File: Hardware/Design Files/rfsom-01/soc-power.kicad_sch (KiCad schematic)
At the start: 55 parts

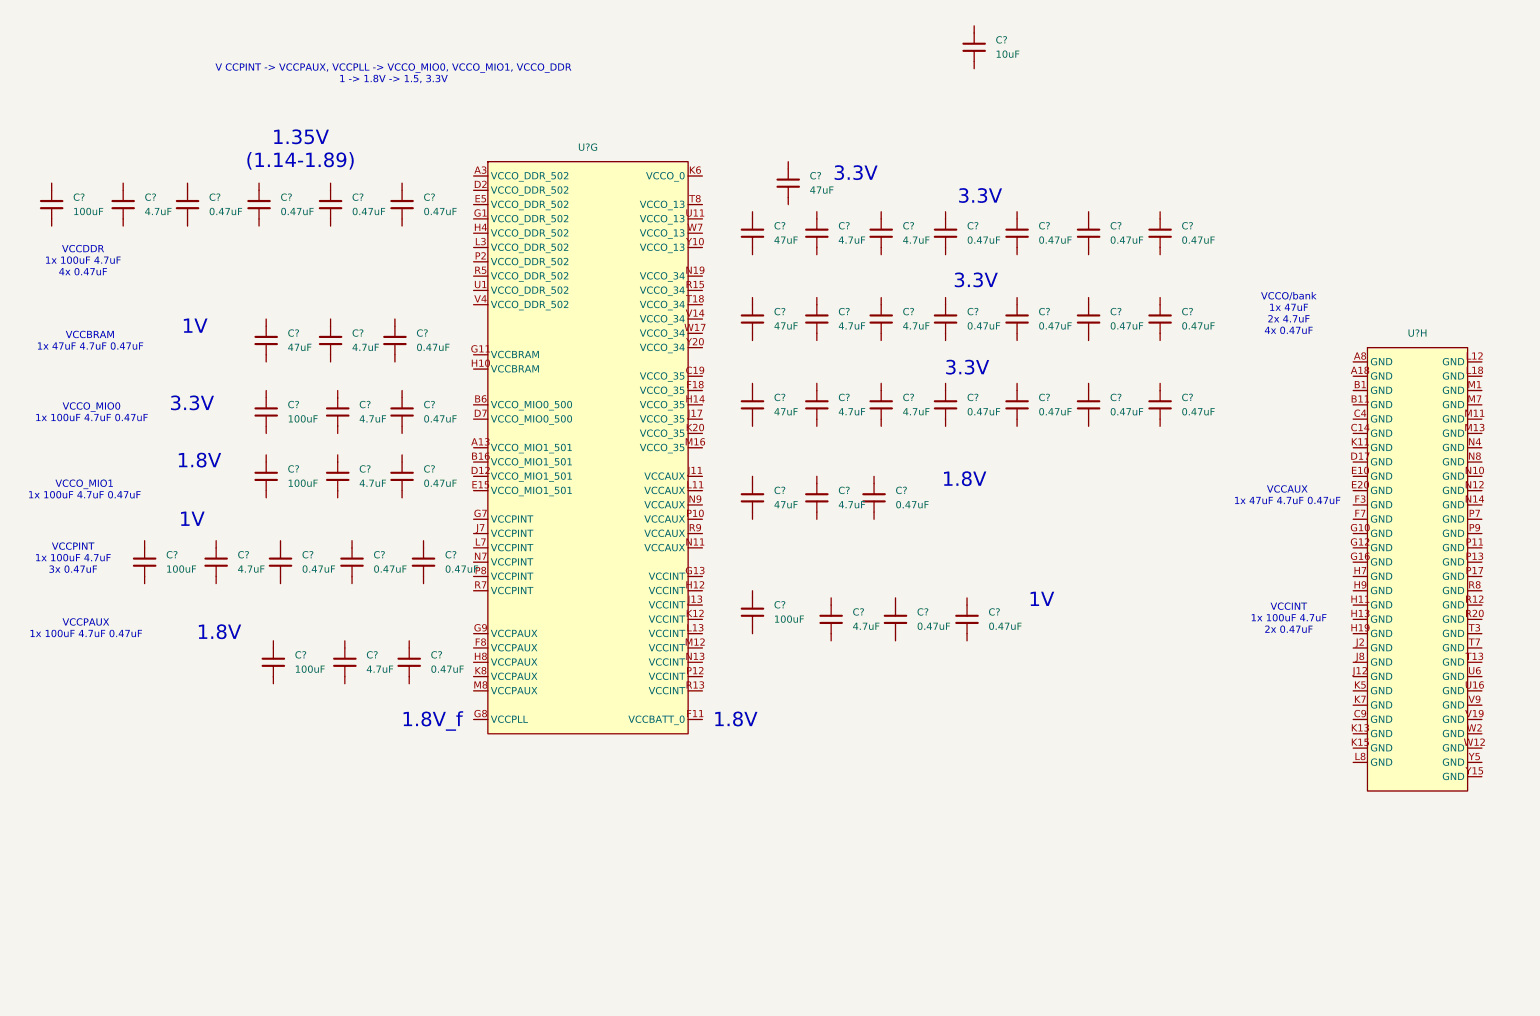
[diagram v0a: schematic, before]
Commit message: ddr progress; added more conns;
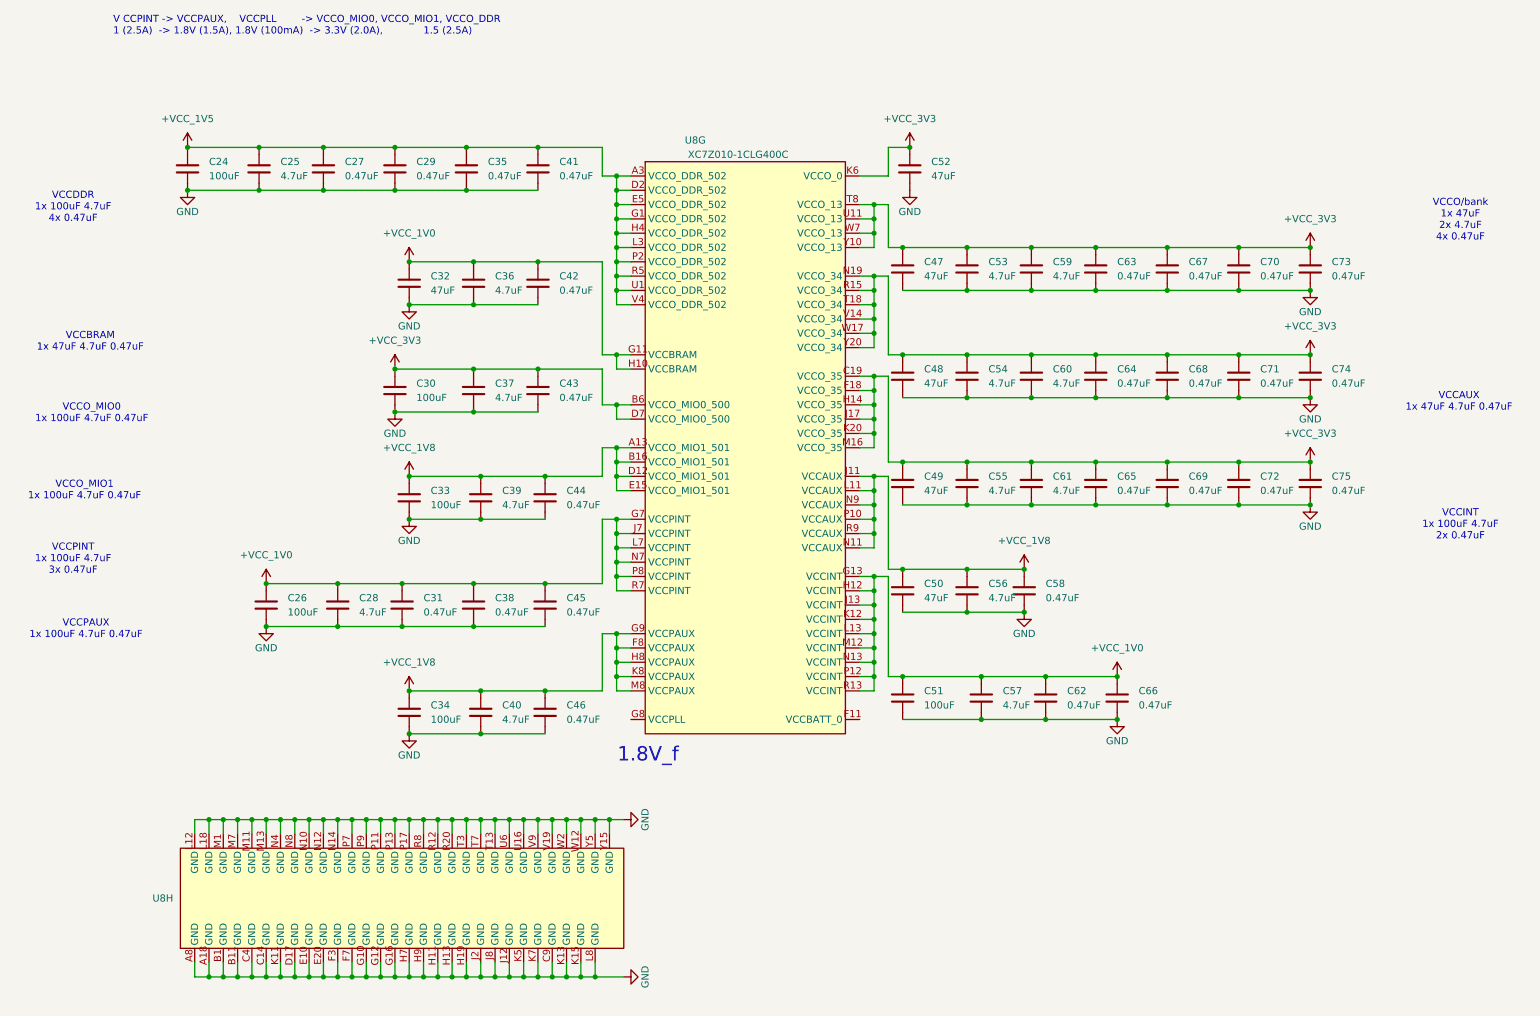
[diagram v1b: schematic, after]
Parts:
- removed C?: GRM188R60G106ME47, Capacitor_SMD:C_0603_1608Metric, symbol Capacitors:GRM188R60G106ME47
- U8: renamed from U?; footprint Package_BGA:Xilinx_CLG400 -> ICs:CLG400
- gave numbers to parts that had none: 53
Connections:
- net +VCC_3V3: now reaches C74.1
- net +VCC_3V3: now also C30.1, C37.1, C43.1, C47.1, C48.1, C49.1, C52.1, C53.1, C54.1, C55.1, C59.1, C60.1, C61.1, C63.1, C64.1, C65.1, C67.1, C68.1, C69.1, C70.1, C71.1, C72.1, C73.1, C75.1, U8.B6 (VCCO_MIO0_500), U8.C19 (VCCO_35), U8.D7 (VCCO_MIO0_500), U8.F18 (VCCO_35), U8.H14 (VCCO_35), U8.J17 (VCCO_35), U8.K20 (VCCO_35), U8.K6 (VCCO_0), U8.M16 (VCCO_35), U8.N19 (VCCO_34), U8.R15 (VCCO_34), U8.T18 (VCCO_34), U8.T8 (VCCO_13), U8.U11 (VCCO_13), U8.V14 (VCCO_34), U8.W17 (VCCO_34), U8.W7 (VCCO_13), U8.Y10 (VCCO_13), U8.Y20 (VCCO_34)
- net GND: now reaches C74.2
- net GND: now also C24.2, C25.2, C26.2, C27.2, C28.2, C29.2, C30.2, C31.2, C32.2, C33.2, C34.2, C35.2, C36.2, C37.2, C38.2, C39.2, C40.2, C41.2, C42.2, C43.2, C44.2, C45.2, C46.2, C47.2, C48.2, C49.2, C50.2, C51.2, C52.2, C53.2, C54.2, C55.2, C56.2, C57.2, C58.2, C59.2, C60.2, C61.2, C62.2, C63.2, C64.2, C65.2, C66.2, C67.2, C68.2, C69.2, C70.2, C71.2, C72.2, C73.2, C75.2, U8.A18 (GND), U8.A8 (GND), U8.B1 (GND), U8.B11 (GND), U8.C14 (GND), U8.C4 (GND), U8.C9 (GND), U8.D17 (GND), U8.E10 (GND), U8.E20 (GND), U8.F3 (GND), U8.F7 (GND), U8.G10 (GND), U8.G12 (GND), U8.G16 (GND), U8.H11 (GND), U8.H13 (GND), U8.H19 (GND), U8.H7 (GND), U8.H9 (GND), U8.J12 (GND), U8.J2 (GND), U8.J8 (GND), U8.K11 (GND), U8.K13 (GND), U8.K15 (GND), U8.K5 (GND), U8.K7 (GND), U8.L12 (GND), U8.L18 (GND), U8.L8 (GND), U8.M1 (GND), U8.M11 (GND), U8.M13 (GND), U8.M7 (GND), U8.N10 (GND), U8.N12 (GND), U8.N14 (GND), U8.N4 (GND), U8.N8 (GND), U8.P11 (GND), U8.P13 (GND), U8.P17 (GND), U8.P7 (GND), U8.P9 (GND), U8.R12 (GND), U8.R20 (GND), U8.R8 (GND), U8.T13 (GND), U8.T3 (GND), U8.T7 (GND), U8.U16 (GND), U8.U6 (GND), U8.V19 (GND), U8.V9 (GND), U8.W12 (GND), U8.W2 (GND), U8.Y15 (GND), U8.Y5 (GND)
- net +VCC_1V5: now reaches C41.1
- net +VCC_1V5: now also C24.1, C25.1, C27.1, C29.1, C35.1, U8.A3 (VCCO_DDR_502), U8.D2 (VCCO_DDR_502), U8.E5 (VCCO_DDR_502), U8.G1 (VCCO_DDR_502), U8.H4 (VCCO_DDR_502), U8.L3 (VCCO_DDR_502), U8.P2 (VCCO_DDR_502), U8.R5 (VCCO_DDR_502), U8.U1 (VCCO_DDR_502), U8.V4 (VCCO_DDR_502)
- net +VCC_1V8: now reaches C33.1
- net +VCC_1V8: now also C34.1, C39.1, C40.1, C44.1, C46.1, C50.1, C56.1, C58.1, U8.A13 (VCCO_MIO1_501), U8.B16 (VCCO_MIO1_501), U8.D12 (VCCO_MIO1_501), U8.E15 (VCCO_MIO1_501), U8.F8 (VCCPAUX), U8.G9 (VCCPAUX), U8.H8 (VCCPAUX), U8.J11 (VCCAUX), U8.K8 (VCCPAUX), U8.L11 (VCCAUX), U8.M8 (VCCPAUX), U8.N11 (VCCAUX), U8.N9 (VCCAUX), U8.P10 (VCCAUX), U8.R9 (VCCAUX)
- net +VCC_1V0: now reaches C42.1
- net +VCC_1V0: now also C26.1, C28.1, C31.1, C32.1, C36.1, C38.1, C45.1, C51.1, C57.1, C62.1, C66.1, U8.G11 (VCCBRAM), U8.G13 (VCCINT), U8.G7 (VCCPINT), U8.H10 (VCCBRAM), U8.H12 (VCCINT), U8.J13 (VCCINT), U8.J7 (VCCPINT), U8.K12 (VCCINT), U8.L13 (VCCINT), U8.L7 (VCCPINT), U8.M12 (VCCINT), U8.N13 (VCCINT), U8.N7 (VCCPINT), U8.P12 (VCCINT), U8.P8 (VCCPINT), U8.R13 (VCCINT), U8.R7 (VCCPINT)
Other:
- note added: "V CCPINT -> VCCPAUX, VCCPLL -> VCCO_MIO0, VCCO_MIO1, VCCO_DDR 1 (2.5A) -> 1.8V (1.5A), 1.8V (100mA) -> 3.3V (2.0A), 1.5 (2.5A)"
- note removed: "1.35V (1.14-1.89)"
- note removed: "1.8V"
- note removed: "1V"
- note removed: "3.3V"
- note removed: "V CCPINT -> VCCPAUX, VCCPLL -> VCCO_MIO0, VCCO_MIO1, VCCO_DDR 1 -> 1.8V -> 1.5, 3.3V"
- moved on the sheet: C24, C25, C26, C27, C28, C29, C30, C31, C32, C33, C34, C35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

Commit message: some ddr routing progress; layerstack per pcbway standard options, review reqd; commit prior to ddr split;
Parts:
- added C163: GRM188R70J474KA01D, Capacitor_SMD:C_0603_1608Metric, symbol Capacitors:GRM188R70J474KA01D
- renumbered C72 to C100, C73 to C101, C74 to C102, C75 to C103, C24 to C46, C25 to C47, C26 to C48, C27 to C49, C28 to C50, C29 to C51, C30 to C52, C31 to C53, C32 to C54, C33 to C55, C34 to C56, C35 to C57, C36 to C58, C37 to C59, C38 to C60, C39 to C61, C40 to C62, C41 to C63, C42 to C64, C43 to C65, C44 to C66, C45 to C67, C46 to C68, C47 to C69, C48 to C70, C49 to C71, C50 to C72, C51 to C73, C52 to C74, C53 to C75, C54 to C82, C55 to C83, C56 to C84, C57 to C85, C58 to C86, C59 to C87, C60 to C88, C61 to C89, C62 to C90, C63 to C91, C64 to C92, C65 to C93, C66 to C94, C67 to C95, C68 to C96, C69 to C97, C70 to C98, C71 to C99, U8 to U5
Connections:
- net +VCC_1V8: now also U5.G8 (VCCPLL), C163.1
- net GND: now also C163.2
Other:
- moved on the sheet: U5H

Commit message: added starage, usb sch; more design progress in sch;
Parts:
- added unit 9 of U5
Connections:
- net +VCC_1V0: no longer U5.G11 (VCCBRAM), U5.H10 (VCCBRAM)
- no-connect marks 0 -> 25

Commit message: updated sch pdf; routign progress;
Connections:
- net +VCC_1V0: now also U5.G11 (VCCBRAM), U5.H10 (VCCBRAM)
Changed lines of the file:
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@@
+	)
+	(junction
+		(at 119.38 78.74)
+		(diameter 0)
+		(color 0 0 0 0)
 	)
 	(junction
@@
 	(junction
 		(at 204.47 60.96)
-		(diameter 0)
-		(color 0 0 0 0)
-	)
-	(junction
-		(at 119.38 80.01)
 		(diameter 0)
 		(color 0 0 0 0)
@@
 	(wire
 		(pts
-			(xy 119.38 80.01) (xy 121.92 80.01)
+			(xy 119.38 78.74) (xy 121.92 78.74)
 		)
 		(stroke
@@
 	(wire
 		(pts
-			(xy 119.38 82.55) (xy 121.92 82.55)
+			(xy 119.38 81.28) (xy 121.92 81.28)
 		)
 		(stroke
@@
 	(wire
 		(pts
-			(xy 119.38 80.01) (xy 119.38 82.55)
-		)
-		(stroke
-			(width 0)
-			(type default)
-		)
-	)
-	(wire
-		(pts
 			(xy 119.38 91.44) (xy 121.92 91.44)
 		)
@@
 	(wire
 		(pts
+			(xy 119.38 78.74) (xy 119.38 81.28)
+		)
+		(stroke
+			(width 0)
+			(type default)
+		)
+	)
+	(wire
+		(pts
 			(xy 193.04 80.01) (xy 181.61 80.01)
 		)
@@
 	(wire
 		(pts
-			(xy 119.38 80.01) (xy 116.84 80.01)
+			(xy 119.38 78.74) (xy 116.84 78.74)
 		)
 		(stroke
@@
 	(wire
 		(pts
-			(xy 116.84 80.01) (xy 116.84 63.5)
-		)
-		(stroke
+			(xy 116.84 78.74) (xy 116.84 63.5)
+		)
+		(stroke

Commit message: replaced pmic;
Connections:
- net +VCC_1V5 renamed +VCC_DDR_1V5
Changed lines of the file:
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@@
 		(on_board yes)
 		(dnp no)
-		(fields_autoplaced yes)
 		(property "Reference" "#PWR012"
 			(at 43.18 46.99 0)
@@
 			)
 		)
-		(property "Value" "+VCC_1V5"
-			(at 43.18 38.1 0)
+		(property "Value" "+VCC_DDR_1V5"
+			(at 35.56 38.354 0)
 			(effects
 				(font
 					(size 1.27 1.27)
 				)
+				(justify left)
 			)
 		)
